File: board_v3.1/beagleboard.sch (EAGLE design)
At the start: 36 parts, among them U1 DWM1000

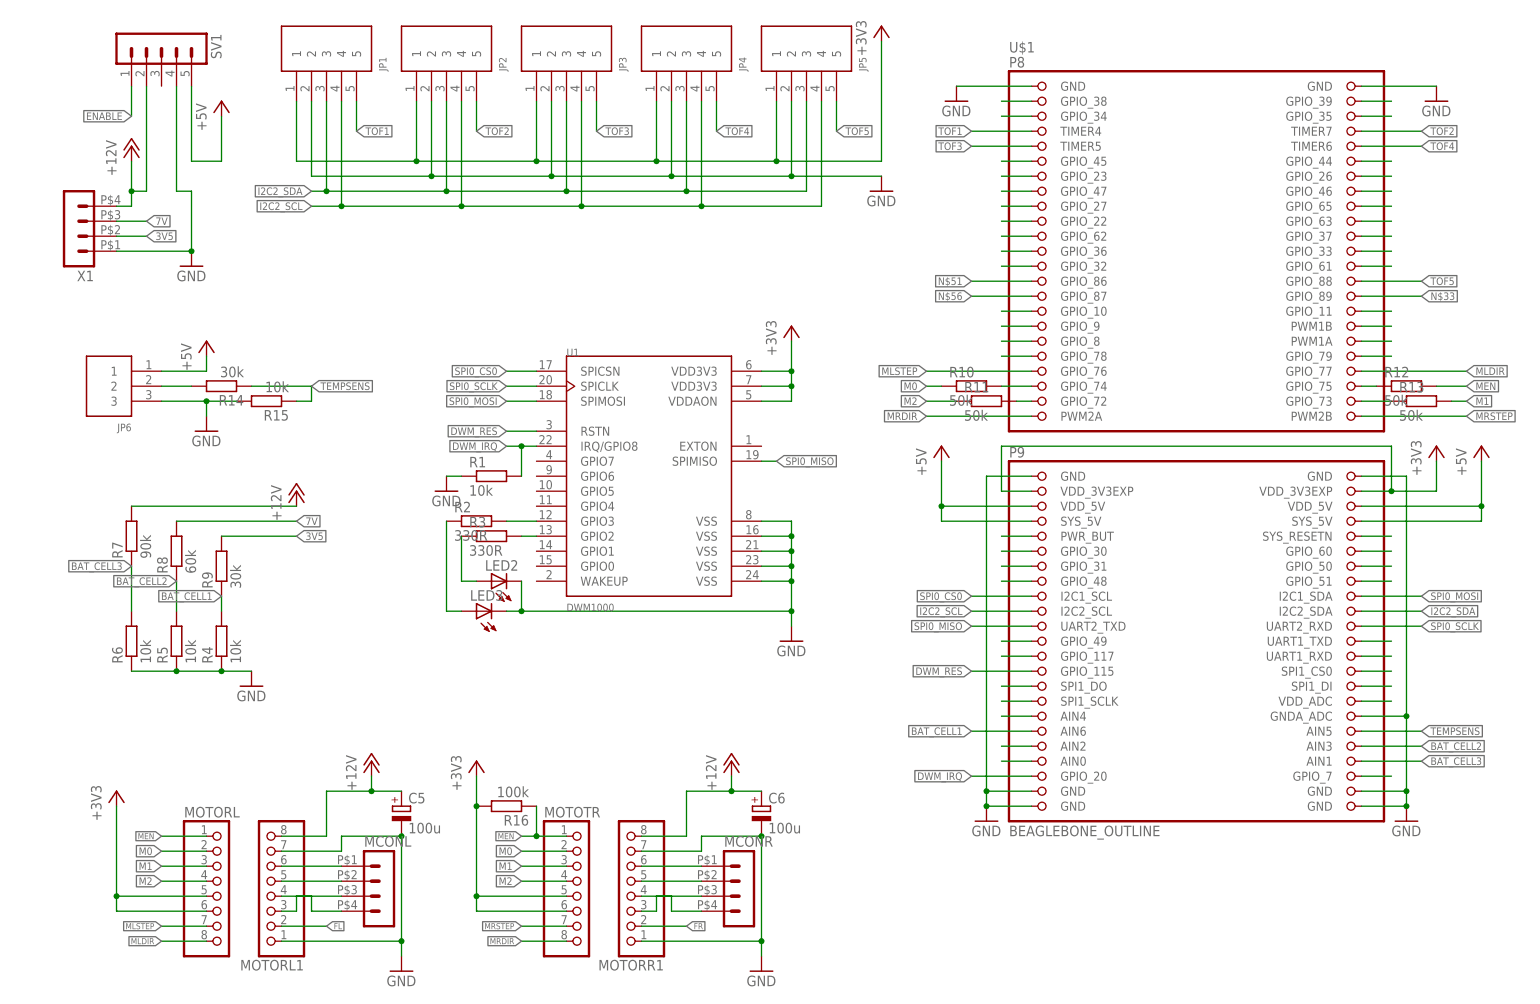
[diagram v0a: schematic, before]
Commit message: board v3.1 beta 5: przepięte 2 TOF i MEN,M0,M1,M2, usunięte rezystory z tych linii, rerouting
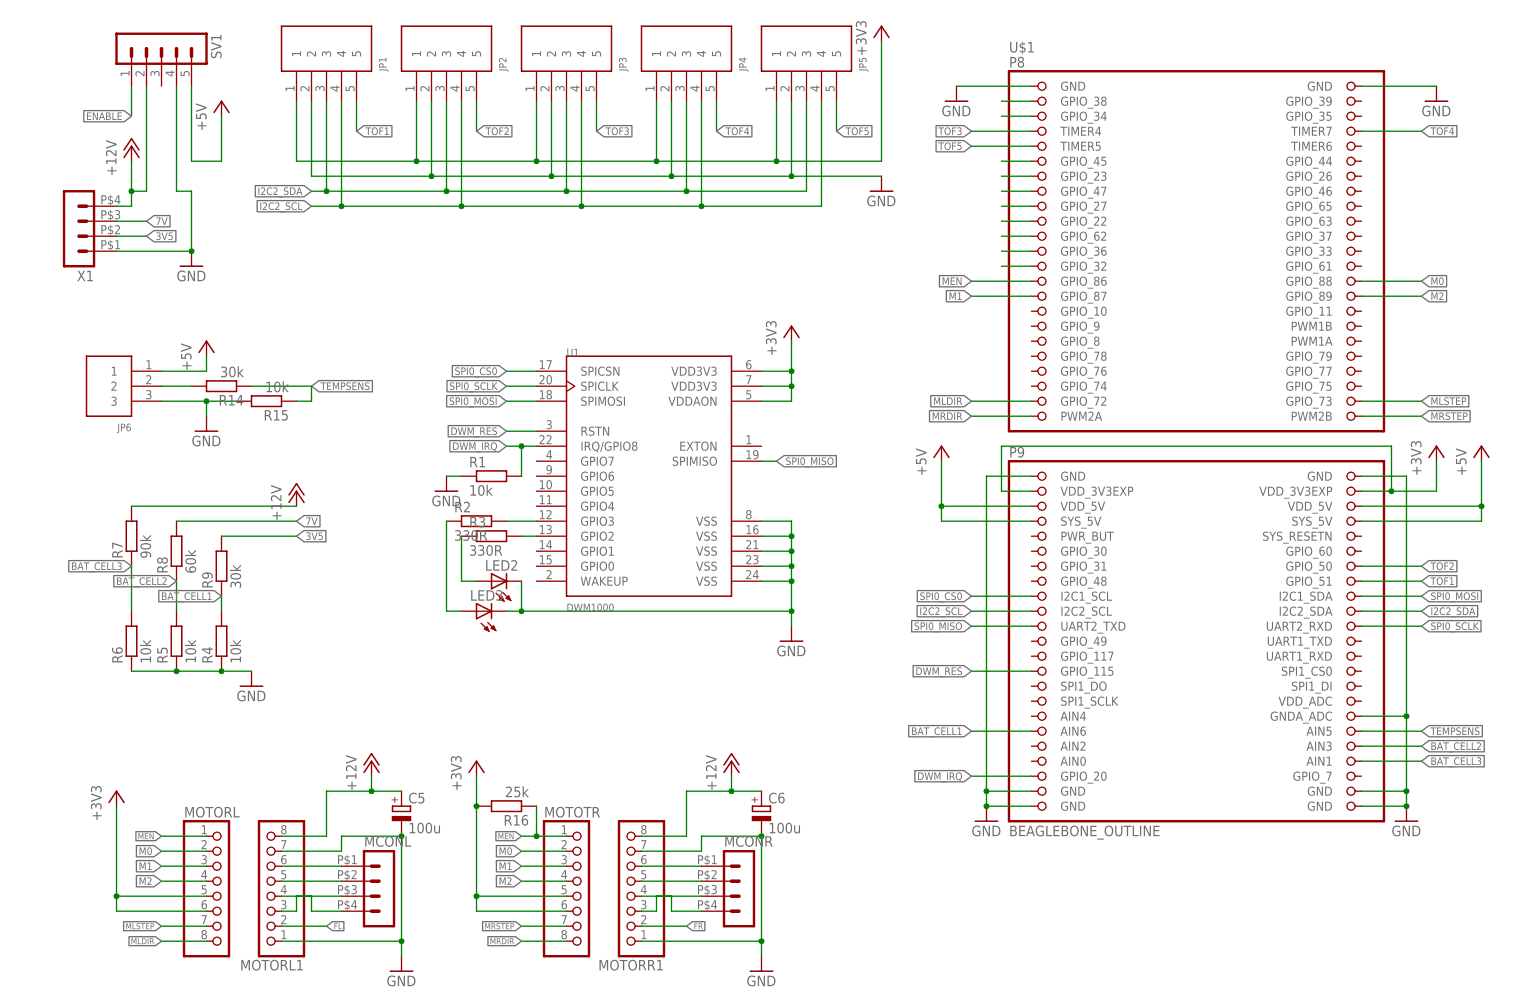
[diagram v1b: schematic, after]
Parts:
- removed R10, R11, R12, R13: 50k, rcl:R-EU_R0603
- R16: value 100k -> 25k
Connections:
- removed net D4ECHO: U$1.AIN0
- removed net D4TRIG: U$1.AIN2
- removed net N$104: U$1.AIN4
- removed net N$16: U$1.SPI1_SCLK
- removed net N$18: U$1.GPIO_39
- removed net N$20: U$1.GPIO_44
- removed net N$21: U$1.GPIO_35
- removed net N$22: U$1.GPIO_46
- removed net N$23: U$1.GPIO_78
- removed net N$24: R13.1, U$1.GPIO_73
- removed net N$25: U$1.GPIO_26
- removed net N$27: U$1.GPIO_65
- removed net N$28: U$1.GPIO_63
- removed net N$29: U$1.GPIO_37
- removed net N$30: U$1.GPIO_33
- removed net N$31: U$1.GPIO_61
- removed net N$33: U$1.GPIO_89
- removed net N$34: U$1.GPIO_11
- removed net N$35: U$1.PWM1B
- removed net N$36: U$1.PWM1A
- removed net N$37: U$1.GPIO_79
- removed net N$39: U$1.PWR_BUT
- removed net N$4: R10.2, U$1.GPIO_74
- removed net N$40: U$1.SPI1_DO
- removed net N$41: U$1.GPIO_30
- removed net N$42: U$1.SPI1_DI
- removed net N$43: U$1.SPI1_CS0
- removed net N$51: U$1.GPIO_86
- removed net N$53: U$1.GPIO_31
- removed net N$54: U$1.GPIO_48
- removed net N$55: U$1.GPIO_117
- removed net N$56: U$1.GPIO_87
- removed net N$57: U$1.GPIO_10
- removed net N$58: U$1.GPIO_9
- removed net N$59: U$1.GPIO_8
- removed net N$62: U$1.SYS_RESETN
- removed net N$63: U$1.GPIO_60
- removed net N$64: U$1.GPIO_50
- removed net N$65: U$1.GPIO_51
- removed net N$7: R11.2, U$1.GPIO_72
- removed net N$70: U$1.VDD_ADC
- removed net N$72: U$1.UART1_TXD
- removed net N$73: U$1.UART1_RXD
- removed net N$75: U$1.GPIO_49
- removed net N$77: U$1.GPIO_7
- removed net N$8: R12.1, U$1.GPIO_75
- net M0: now also U$1.GPIO_88; no longer R10.1
- net M1: now also U$1.GPIO_87; no longer R13.2
- net M2: now also U$1.GPIO_89; no longer R11.1
- net MEN: now also U$1.GPIO_86; no longer R12.2
- net MLDIR: now also U$1.GPIO_72; no longer U$1.GPIO_77
- net MLSTEP: now also U$1.GPIO_73; no longer U$1.GPIO_76
- net TOF1: now also U$1.GPIO_51; no longer U$1.TIMER4
- net TOF2: now also U$1.GPIO_50; no longer U$1.TIMER7
- net TOF3: now also U$1.TIMER4; no longer U$1.TIMER5
- net TOF4: now also U$1.TIMER7; no longer U$1.TIMER6
- net TOF5: now also U$1.TIMER5; no longer U$1.GPIO_88

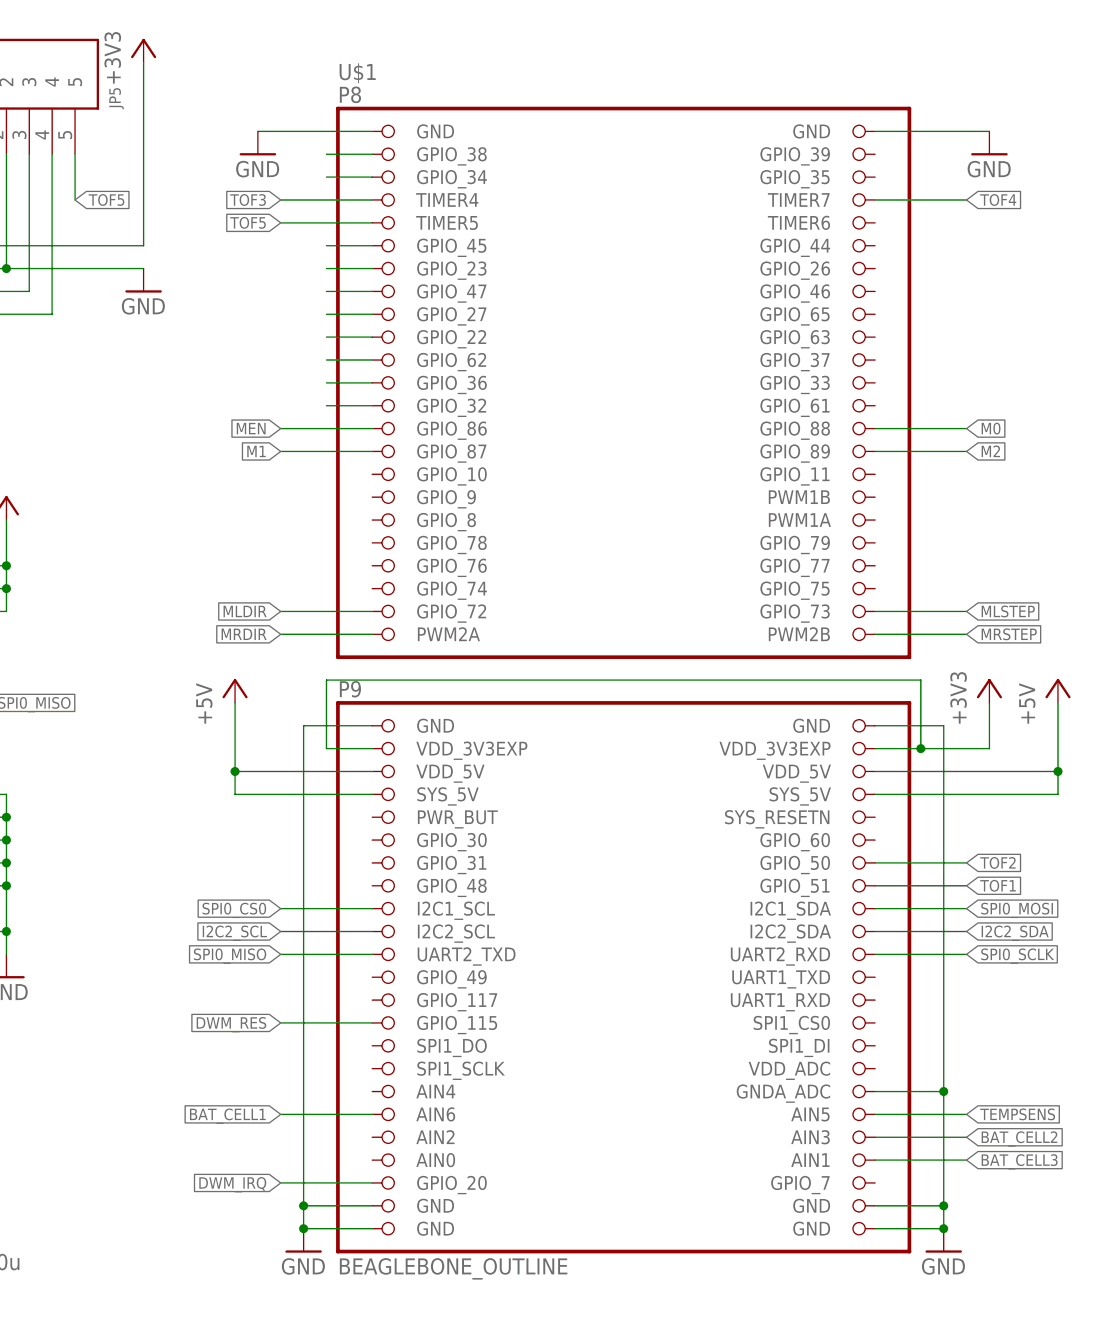
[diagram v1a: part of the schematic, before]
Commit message: board v3.1 beta 6: poprawione dzielniki napięcia baterii na płytce
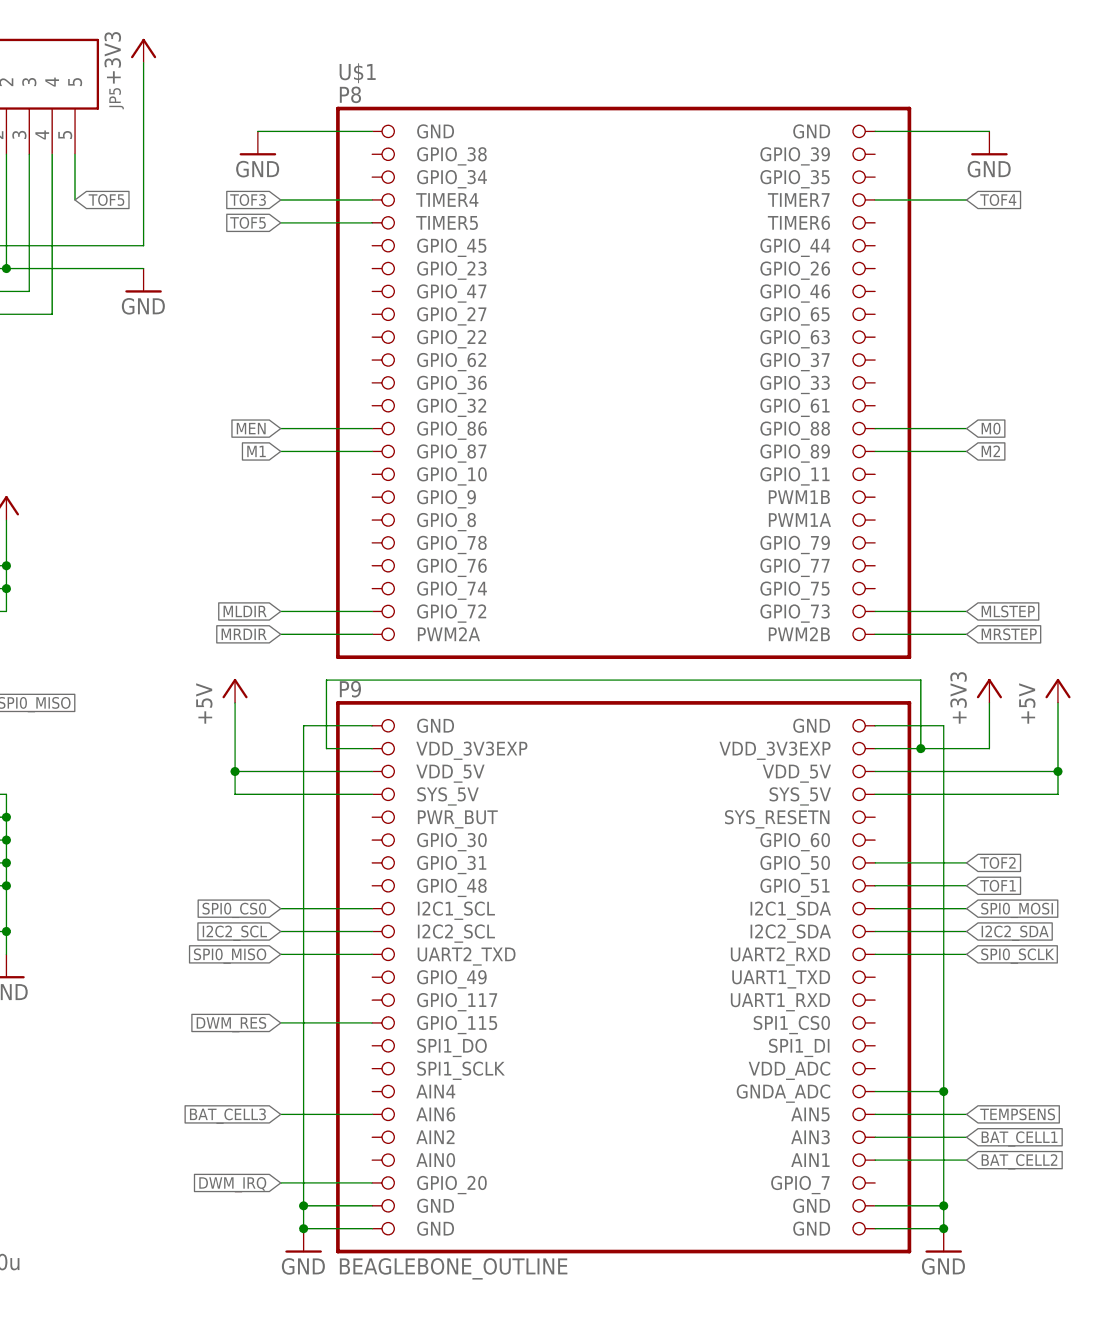
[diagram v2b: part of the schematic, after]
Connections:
- removed net N$17: U$1.GPIO_38
- removed net N$19: U$1.GPIO_34
- removed net N$26: U$1.GPIO_47
- removed net N$38: U$1.GPIO_45
- removed net N$44: U$1.GPIO_23
- removed net N$46: U$1.GPIO_27
- removed net N$47: U$1.GPIO_22
- removed net N$48: U$1.GPIO_62
- removed net N$49: U$1.GPIO_36
- removed net N$50: U$1.GPIO_32
- net BAT_CELL1: now also U$1.AIN3; no longer U$1.AIN6
- net BAT_CELL2: now also U$1.AIN1; no longer U$1.AIN3
- net BAT_CELL3: now also U$1.AIN6; no longer U$1.AIN1
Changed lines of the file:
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@@
 </segment>
 <segment>
-<pinref part="U$1" gate="G$1" pin="AIN3"/>
-<wire x1="195.58" y1="7.62" x2="205.74" y2="7.62" width="0.1524" layer="91"/>
-<label x="205.74" y="7.62" size="1.27" layer="95" xref="yes"/>
-</segment>
-</net>
-<net name="N$17" class="0">
-<segment>
-<pinref part="U$1" gate="G$1" pin="GPIO_38"/>
-<wire x1="139.7" y1="116.84" x2="134.62" y2="116.84" width="0.1524" layer="91"/>
-</segment>
-</net>
-<net name="N$19" class="0">
-<segment>
-<pinref part="U$1" gate="G$1" pin="GPIO_34"/>
-<wire x1="139.7" y1="114.3" x2="134.62" y2="114.3" width="0.1524" layer="91"/>
-</segment>
-</net>
-<net name="N$44" class="0">
-<segment>
-<pinref part="U$1" gate="G$1" pin="GPIO_23"/>
-<wire x1="139.7" y1="104.14" x2="134.62" y2="104.14" width="0.1524" layer="91"/>
-</segment>
-</net>
-<net name="N$46" class="0">
-<segment>
-<pinref part="U$1" gate="G$1" pin="GPIO_27"/>
-<wire x1="139.7" y1="99.06" x2="134.62" y2="99.06" width="0.1524" layer="91"/>
-</segment>
-</net>
-<net name="N$47" class="0">
-<segment>
-<pinref part="U$1" gate="G$1" pin="GPIO_22"/>
-<wire x1="139.7" y1="96.52" x2="134.62" y2="96.52" width="0.1524" layer="91"/>
-</segment>
-</net>
-<net name="N$48" class="0">
-<segment>
-<pinref part="U$1" gate="G$1" pin="GPIO_62"/>
-<wire x1="139.7" y1="93.98" x2="134.62" y2="93.98" width="0.1524" layer="91"/>
-</segment>
-</net>
-<net name="N$49" class="0">
-<segment>
-<pinref part="U$1" gate="G$1" pin="GPIO_36"/>
-<wire x1="139.7" y1="91.44" x2="134.62" y2="91.44" width="0.1524" layer="91"/>
-</segment>
-</net>
-<net name="N$50" class="0">
-<segment>
-<pinref part="U$1" gate="G$1" pin="GPIO_32"/>
-<wire x1="139.7" y1="88.9" x2="134.62" y2="88.9" width="0.1524" layer="91"/>
+<pinref part="U$1" gate="G$1" pin="AIN1"/>
+<wire x1="195.58" y1="5.08" x2="205.74" y2="5.08" width="0.1524" layer="91"/>
+<label x="205.74" y="5.08" size="1.27" layer="95" xref="yes"/>
 </segment>
 </net>
@@
 </segment>
 </net>
-<net name="N$26" class="0">
-<segment>
-<pinref part="U$1" gate="G$1" pin="GPIO_47"/>
-<wire x1="139.7" y1="101.6" x2="134.62" y2="101.6" width="0.1524" layer="91"/>
-</segment>
-</net>
 <net name="TOF1" class="0">
 <segment>
@@
 </segment>
 </net>
-<net name="N$38" class="0">
-<segment>
-<pinref part="U$1" gate="G$1" pin="GPIO_45"/>
-<wire x1="139.7" y1="106.68" x2="134.62" y2="106.68" width="0.1524" layer="91"/>
-</segment>
-</net>
 <net name="SPI0_CS0" class="0">
 <segment>
@@
 <net name="BAT_CELL3" class="0">
 <segment>
-<pinref part="U$1" gate="G$1" pin="AIN1"/>
-<wire x1="195.58" y1="5.08" x2="205.74" y2="5.08" width="0.1524" layer="91"/>
-<label x="205.74" y="5.08" size="1.27" layer="95" xref="yes"/>
-</segment>
-<segment>
 <wire x1="-12.7" y1="38.1" x2="-12.7" y2="30.48" width="0.1524" layer="91"/>
 <pinref part="R6" gate="G$1" pin="2"/>
@@
 <pinref part="R7" gate="G$1" pin="1"/>
 </segment>
-</net>
-<net name="BAT_CELL1" class="0">
 <segment>
 <pinref part="U$1" gate="G$1" pin="AIN6"/>
@@
 <label x="129.54" y="10.16" size="1.27" layer="95" rot="R180" xref="yes"/>
 </segment>
+</net>
+<net name="BAT_CELL1" class="0">
 <segment>
 <wire x1="2.54" y1="33.02" x2="2.54" y2="30.48" width="0.1524" layer="91"/>
@@
 <pinref part="R9" gate="G$1" pin="1"/>
 </segment>
-</net>
+<segment>
+<pinref part="U$1" gate="G$1" pin="AIN3"/>
+<wire x1="195.58" y1="7.62" x2="205.74" y2="7.62" width="0.1524" layer="91"/>
+<label x="205.74" y="7.62" size="1.27" layer="95" xref="yes"/>
+</segment>
+</net>
